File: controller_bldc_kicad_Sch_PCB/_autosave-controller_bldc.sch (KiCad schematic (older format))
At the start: 57 parts, among them J1 Battery Supply, J2 Emergency Button OUT, J3 Emergency Button IN, J4 Brake, J5 Throttle, J6 LM35, J7 Hall Sensors, J8 Nextion Nx3224T028, J9 BLDC Motor, K1 ADW11, Q1 IRF1010N, Q2 IRF1010N, Q3 IRF1010N, Q4 IRF1010N, Q5 IRF1010N, Q6 IRF1010N, SW1 ON_OFF, SW2 OPC, U1 ESP32-DEVKITC-32D, U2 LM317_TO-220, U3 LM7805_TO220, U4 IR2103, U8 IR2103, U9 IR2103

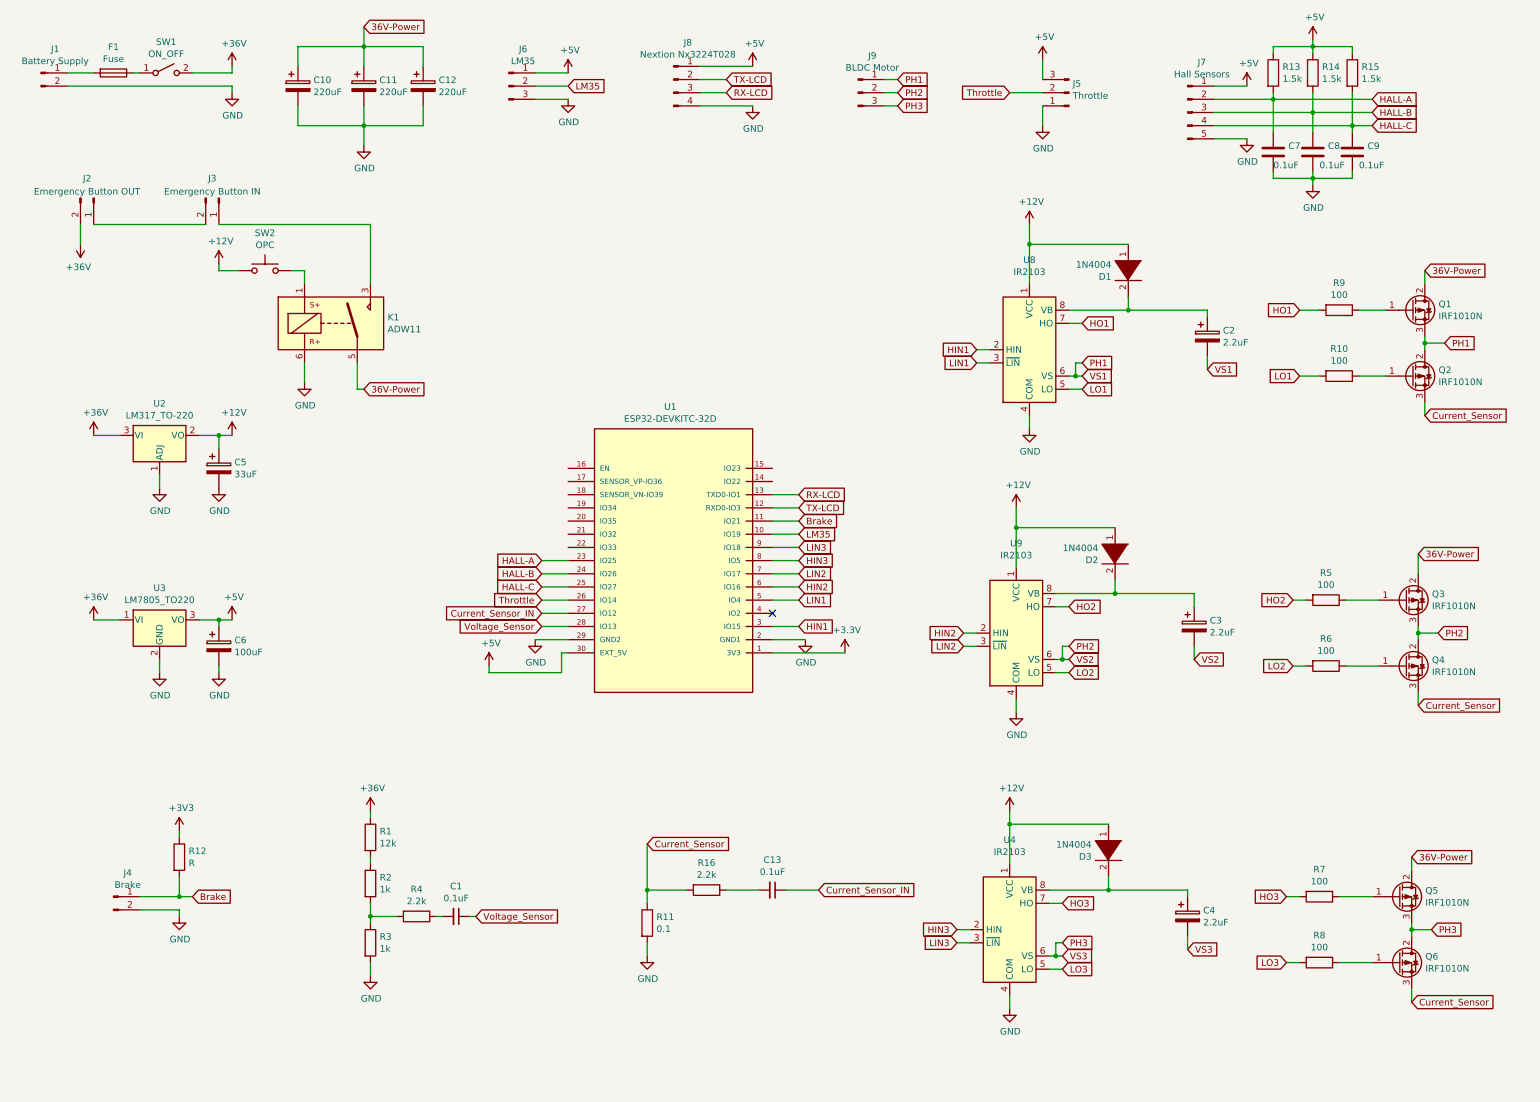
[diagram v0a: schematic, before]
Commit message: PCB: Added Amp Op library and changed V & A Sensors
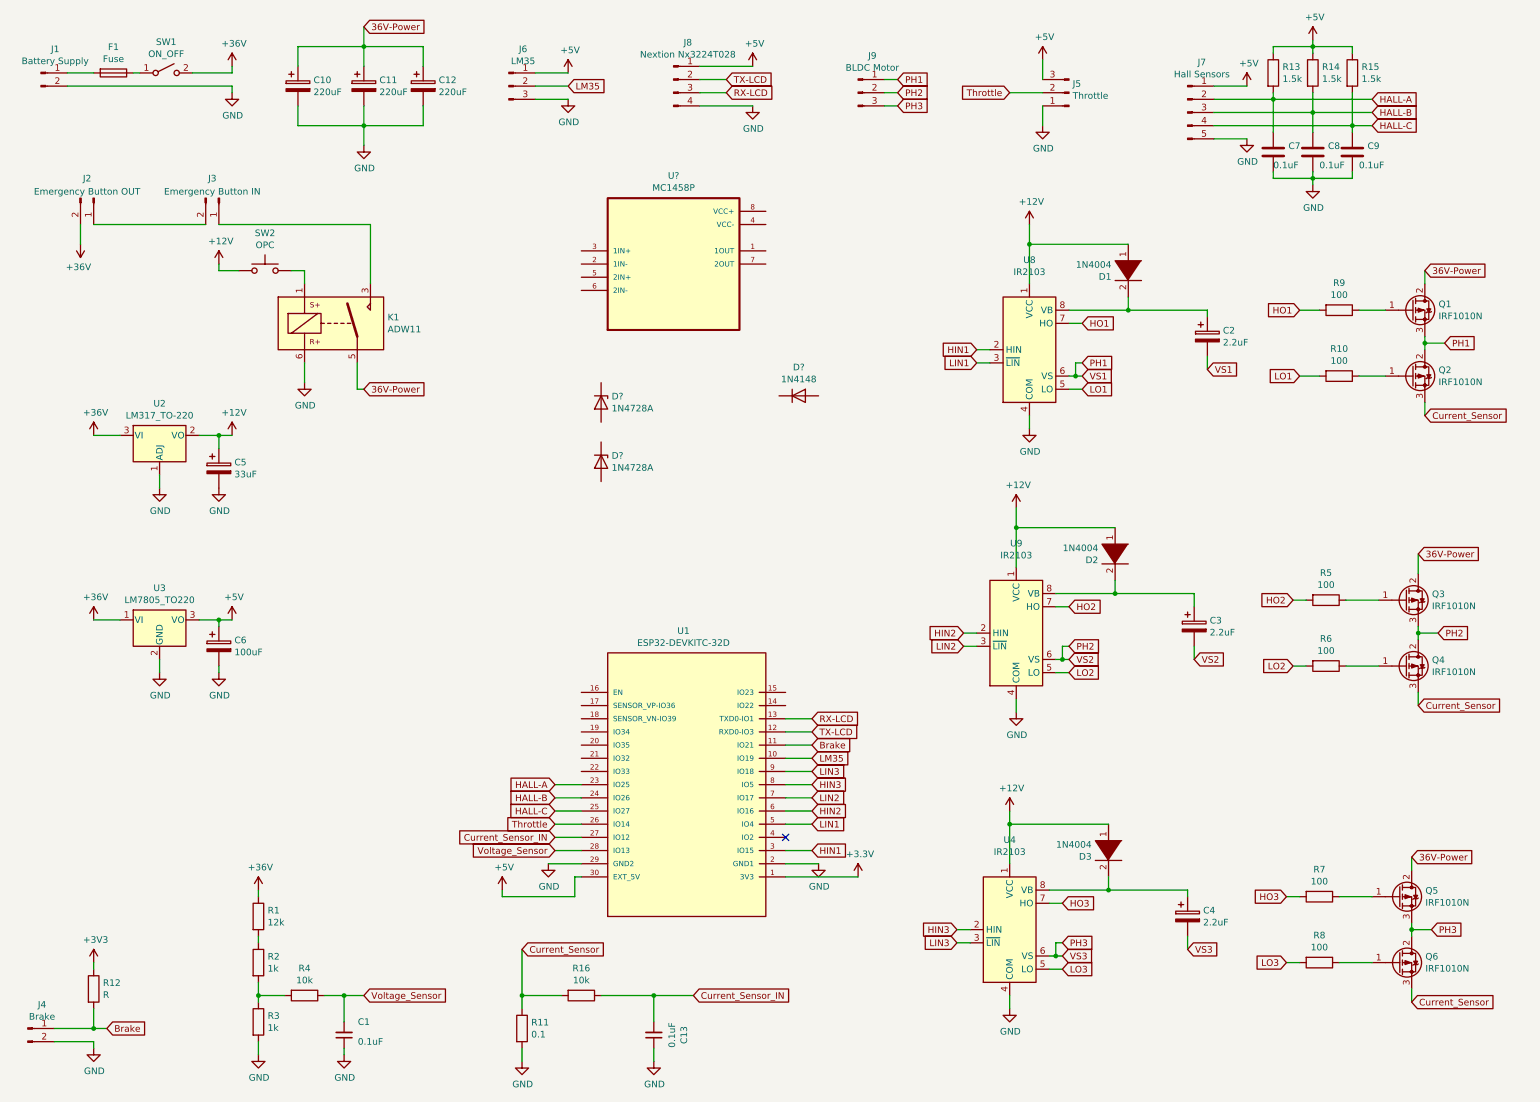
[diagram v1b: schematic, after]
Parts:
- added D? (x2): 1N4728A, Diode_THT:D_DO-41_SOD81_P10.16mm_Horizontal, symbol Diode:1N47xxA
- added D?: 1N4148, Diode_THT:D_DO-35_SOD27_P7.62mm_Horizontal, symbol Diode:1N4148
- added U?: MC1458P, DIP794W45P254L959H508Q8, symbol MC1458P:MC1458P
- R16, R4: value 2.2k -> 10k
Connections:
- net Current_Sensor_IN: now also C13.2, R16.1; no longer C13.1
- net GND: now also C1.1, C13.1
- net Voltage_Sensor: now also C1.2, R4.1; no longer C1.1
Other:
- moved on the sheet: C1, C13, J4, R1, R11, R12, R16, R2, R3, R4, U1
